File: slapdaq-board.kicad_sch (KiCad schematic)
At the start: 20 parts, among them J1 12V POWER IN, Q1 BSS84, U1 LM2675M-3.3, U2 LM2675M-5

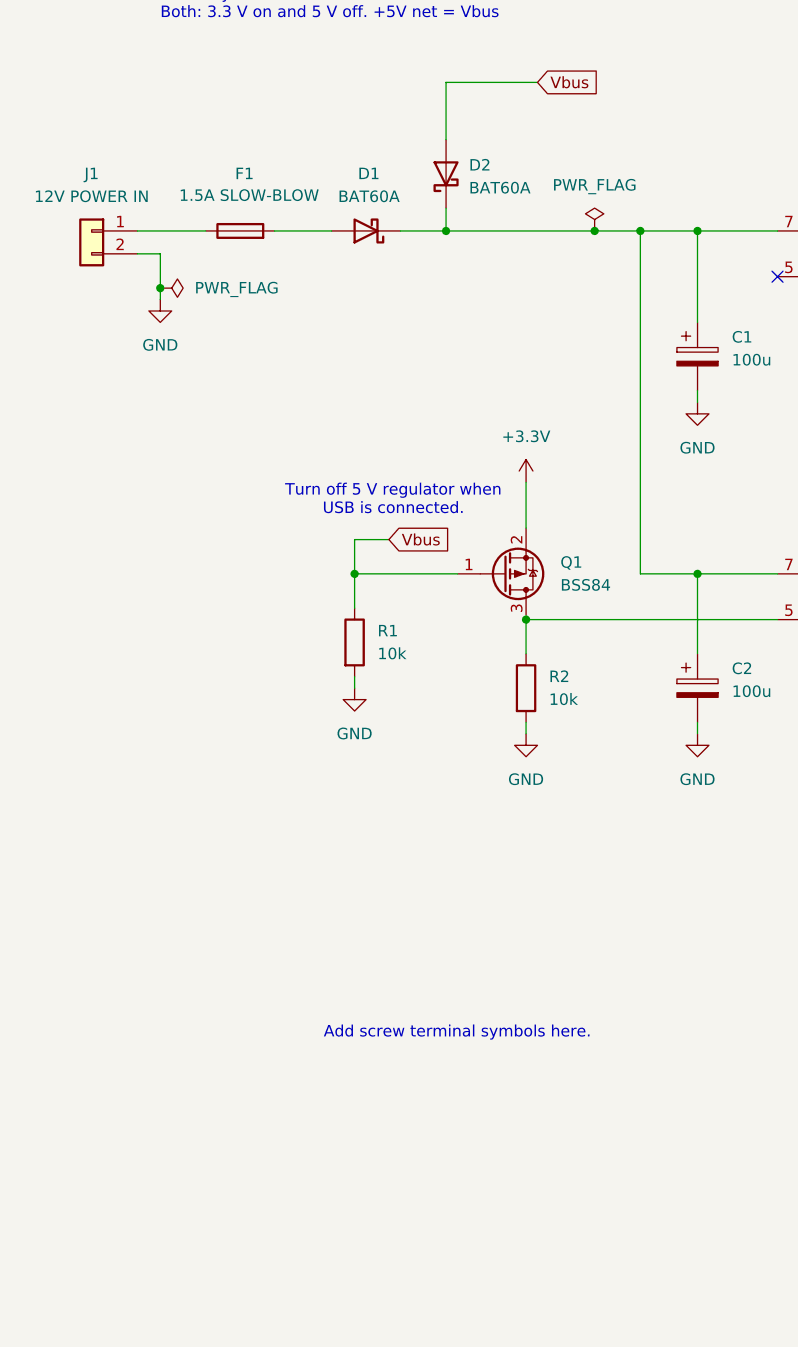
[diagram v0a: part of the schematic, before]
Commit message: Add screw terminals
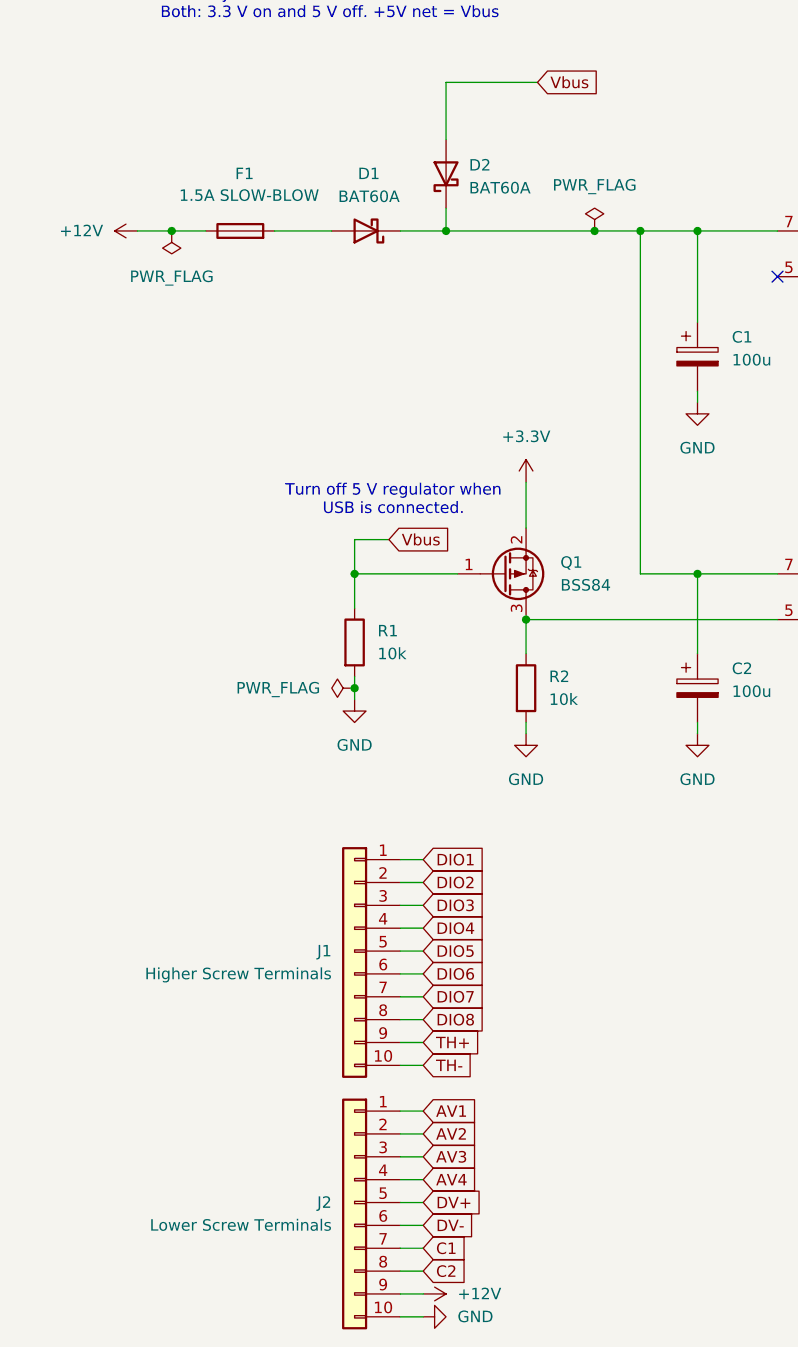
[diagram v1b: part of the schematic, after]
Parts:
- removed J1: 12V POWER IN, symbol Connector_Generic:Conn_01x02
- added J1: Higher Screw Terminals, Custom_Footprints:CONN_SD-39512-001_10P_MOL, symbol Connector_Generic:Conn_01x10
- added J2: Lower Screw Terminals, Custom_Footprints:CONN_SD-39512-001_10P_MOL, symbol Connector_Generic:Conn_01x10
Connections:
- net GND: now also J2.10 (Pin_10)
- net +12V: now reaches F1.1
- net +12V: now also J2.9 (Pin_9)
- new net AV1: J2.1 (Pin_1)
- new net AV2: J2.2 (Pin_2)
- new net AV3: J2.3 (Pin_3)
- new net AV4: J2.4 (Pin_4)
- new net C1: J2.7 (Pin_7)
- new net C2: J2.8 (Pin_8)
- new net DIO1: J1.1 (Pin_1)
- new net DIO2: J1.2 (Pin_2)
- new net DIO3: J1.3 (Pin_3)
- new net DIO4: J1.4 (Pin_4)
- new net DIO5: J1.5 (Pin_5)
- new net DIO6: J1.6 (Pin_6)
- new net DIO7: J1.7 (Pin_7)
- new net DIO8: J1.8 (Pin_8)
- new net DV+: J2.5 (Pin_5)
- new net DV-: J2.6 (Pin_6)
- new net TH+: J1.9 (Pin_9)
- new net TH-: J1.10 (Pin_10)
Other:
- note removed: "Add screw terminal symbols here."

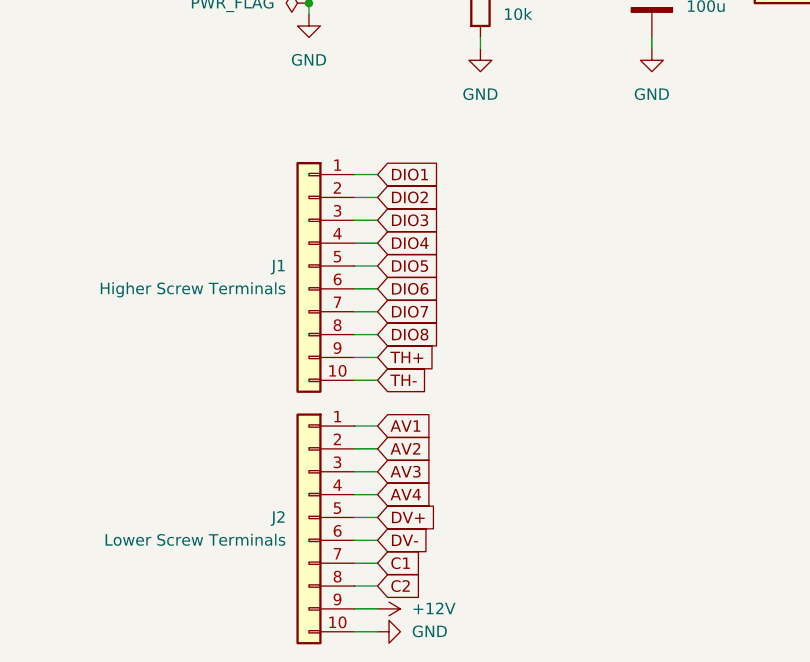
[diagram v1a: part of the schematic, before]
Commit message: Add 3D models and rearrange pins
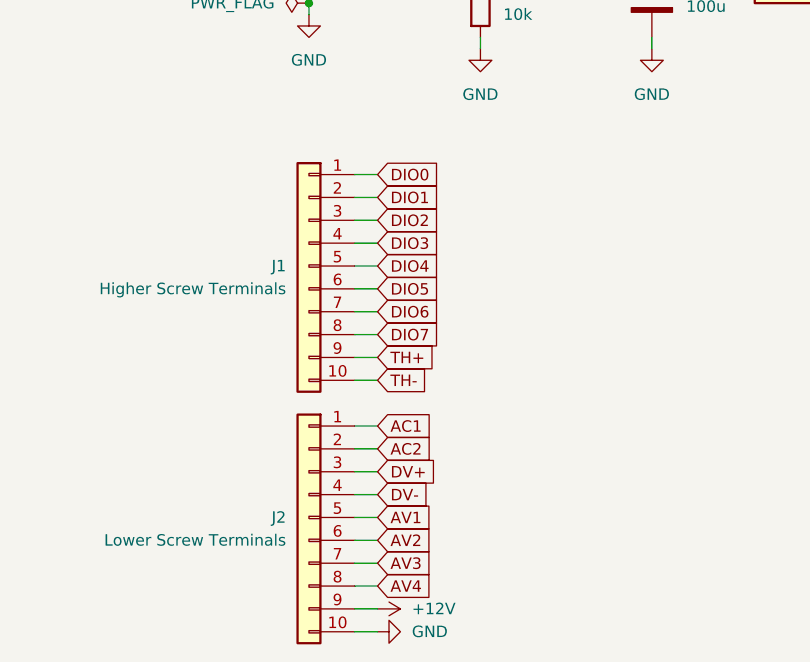
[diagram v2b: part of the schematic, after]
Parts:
- NT1: footprint (none) -> NetTie:NetTie-2_SMD_Pad0.5mm
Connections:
- net C1 is gone; now on net AV3: J2.7 (Pin_7)
- net C2 is gone; now on net AV4: J2.8 (Pin_8)
- net DIO8 is gone; now on net DIO7: J1.8 (Pin_8)
- net AV1: now also J2.5 (Pin_5); no longer J2.1 (Pin_1)
- net AV2: now also J2.6 (Pin_6); no longer J2.2 (Pin_2)
- net AV3: no longer J2.3 (Pin_3)
- net AV4: no longer J2.4 (Pin_4)
- net DIO1: now also J1.2 (Pin_2); no longer J1.1 (Pin_1)
- net DIO2: now also J1.3 (Pin_3); no longer J1.2 (Pin_2)
- net DIO3: now also J1.4 (Pin_4); no longer J1.3 (Pin_3)
- net DIO4: now also J1.5 (Pin_5); no longer J1.4 (Pin_4)
- net DIO5: now also J1.6 (Pin_6); no longer J1.5 (Pin_5)
- net DIO6: now also J1.7 (Pin_7); no longer J1.6 (Pin_6)
- net DIO7: no longer J1.7 (Pin_7)
- net DV+: now also J2.3 (Pin_3); no longer J2.5 (Pin_5)
- net DV-: now also J2.4 (Pin_4); no longer J2.6 (Pin_6)
- new net AC1: J2.1 (Pin_1)
- new net AC2: J2.2 (Pin_2)
- new net DIO0: J1.1 (Pin_1)
